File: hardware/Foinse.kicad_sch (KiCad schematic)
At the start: 150 parts, among them J1 Conn_02x03_Odd_Even, J10 Conn_02x03_Odd_Even, J2 2060-1452, J3 ESQ-110-14-G-D, J4 PJ-002AH, J5 2060-1452/998-404, J8 2601-1108, J9 USB_C_Receptacle_USB2.0_16P, Q1 AO3400A, Q10 AO3400A, Q11 AO3400A, Q12 AO3400A, Q13 AO3400A, Q14 AO3400A, Q2 AO3400A, Q3 AO3400A, Q4 AO3400A, Q5 AO3400A, Q6 AO3400A, Q7 AO3400A, Q8 AO3400A, Q9 AO3400A, U1 STM32F072C8Tx, U10 LTV-817, U11 LTV-817, U12 LTV-817, U13 LTV-817, U14 USBLC6-2SC6, U15 INA239AIDGSR, U16 INA239AIDGSR, U17 LTC4412xS6, U18 LTV-817, U19 TPS56A37RPAR, U2 TLV70433DBVT, U3 LTV-817, U4 TJA1051T-3, U5 TPS563203, U7 LTV-817, U8 LTV-817, U9 LTV-817

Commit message: folders are indded cool
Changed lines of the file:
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@@
 		(exclude_from_sim no)
 		(at 476.25 21.59 0)
-		(size -99.06 260.35)
+		(size 99.06 260.35)
 		(margins 0.9525 0.9525 0.9525 0.9525)
 		(stroke

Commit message: minor changes
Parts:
- removed C30, C31, C33: 1 uF, Capacitor_SMD:C_0402_1005Metric, symbol Device:C
- removed D1, D11, D3, D5, D7: RED LED, LED_SMD:LED_0402_1005Metric, symbol Device:LED
- removed D2, D4, D6, D8: GREEN LED, LED_SMD:LED_0402_1005Metric, symbol Device:LED
- removed J1, J10: Conn_02x03_Odd_Even, Connector_PinHeader_1.00mm:PinHeader_2x03_P1.00mm_Vertical, symbol Connector_Generic:Conn_02x03_Odd_Even
- removed J2: 2060-1452, Foinse Footprints:WAG, symbol Wago_2060-1452 998-404:2060-1452_998-404
- removed J3: ESQ-110-14-G-D, Foinse Footprints:SAMTEC_ESQ-110-14-G-D, symbol ESQ-110-X-X-D:ESQ-110-X-X-D
- removed J5: 2060-1452/998-404, Foinse Footprints:WAG, symbol Wago_2060-1452 998-404:2060-1452_998-404
- removed J8: 2601-1108, Foinse Footprints:CONN8_2601-1108_WAG, symbol Wago_2601-1104:2601-1108
- removed J9: USB_C_Receptacle_USB2.0_16P, Connector_USB:USB_C_Receptacle_G-Switch_GT-USB-7010ASV, symbol Connector:USB_C_Receptacle_USB2.0_16P
- removed Q1, Q10, Q11, Q12, Q13, Q14, Q2, Q3, Q4, Q5, Q6, Q7, Q8, Q9: AO3400A, Package_TO_SOT_SMD:SOT-23, symbol Transistor_FET:AO3400A
- removed R10, R30, R39: 2 kΩ, Resistor_SMD:R_0402_1005Metric, symbol Device:R
- removed R11, R40: 4.7 kΩ, Resistor_SMD:R_0402_1005Metric, symbol Device:R
- removed R12, R14, R16, R23, R25, R32, R34, R48, R6: 10k Ω, Resistor_SMD:R_0402_1005Metric, symbol Device:R
- removed R13, R19, R28, R37: 1k Ω, Resistor_SMD:R_0402_1005Metric, symbol Device:R
- removed R15, R24, R33, R47: 220 Ω, Resistor_SMD:R_0402_1005Metric, symbol Device:R
- removed R18, R22, R27, R31, R36, R49, R8: 4.7k Ω, Resistor_SMD:R_0402_1005Metric, symbol Device:R
- removed R20: 6k Ω, Resistor_SMD:R_0402_1005Metric, symbol Device:R
- removed R21: 2k Ω, Resistor_SMD:R_0402_1005Metric, symbol Device:R
- removed R29, R38, R9: 6 kΩ, Resistor_SMD:R_0402_1005Metric, symbol Device:R
- removed R41, R42: 5.1K, Resistor_SMD:R_0402_1005Metric, symbol Device:R
- removed R43, R44: 10K, Resistor_SMD:R_0402_1005Metric, symbol Device:R
- removed U10, U11, U12, U13, U18, U3, U7, U8, U9: LTV-817, Foinse Footprints:SO4_TOS, symbol Isolator:LTV-817
- removed U14: USBLC6-2SC6, Package_TO_SOT_SMD:SOT-23-6, symbol Power_Protection:USBLC6-2SC6
- added J1: ESQ-110-X-X-D, SAMTEC_ESQ-110-14-G-D, symbol ESQ-110-X-X-D:ESQ-110-X-X-D
- added J2: XT30PW-M, footprints:AMASS_XT30PW-M, symbol XT30PW-M:XT30PW-M
- added J6: JTAG-10 PIN, Connector_IDC:IDC-Header_2x05_P2.54mm_Vertical, symbol Connector_Generic_MountingPin:Conn_01x10_MountingPin
- C32: value 1 uF -> 100nF
- R5: value 220 Ω -> 10kΩ
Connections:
- net Aux1 neg is gone; now on net GND: C32.2
- net VBAT_AUX1 is gone; now on net NRST: C32.1
- net 3.3V: now also J6.7 (Pin_7), J6.8 (Pin_8)
- net GND: now also R5.2, J1.03, J1.04, J1.07, J1.08, J1.14, J1.19, J1.20, J2.N, J6.5 (Pin_5), J6.6 (Pin_6)
- net NRST: now also J1.17, J6.1 (Pin_1)
- net SWDIO: now also J1.15, J6.4 (Pin_4)
- net at MOSFET1.2 (D), U17.1 (VIN): now also J2.P
- net at U1.44 (BOOT0): now also R5.1
- net AUX1_FIRE: no longer names the net of U1.41 (PB5)
- net AUX1_SEAT: no longer names the net of U1.25 (PB12)
- net AUX2_FIRE: no longer names the net of U1.42 (PB6)
- net AUX2_SEAT: no longer names the net of U1.26 (PB13)
- net DROGUE_FIRE: no longer names the net of U1.39 (PB3)
- net DROGUE_FIRE: no longer R5.1
- net DROGUE_SEAT: no longer names the net of U1.21 (PB10)
- net MAIN_FIRE: no longer names the net of U1.40 (PB4)
- net MAIN_SEAT: no longer names the net of U1.22 (PB11)
- net Mode_sel: no longer names the net of U1.45 (PB8)
- net PYRO_ON: no longer names the net of U1.43 (PB7)
- net SWCLK renamed SWCLK3
- net SWCLK3: now also J1.11, J6.2 (Pin_2)
- new net 5V_LOGIC: J1.05, J1.06
- new net 5v_SERVO: J1.01, J1.02
- new net CAN_o+: J1.16
- new net CAN_o-: J1.18
- no-connect marks 6 -> 12
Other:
- note added: "Connector_IDC:IDC-Header_2x05_P2.54mm_Vertical"
- note added: "what is the current and voltage rating for this?"
- note removed: "E-Match Trigger Circuit"
- note removed: "Pyro Connectors"
- note removed: "USB-C"
- note removed: "USB-C & mode select"
- moved on the sheet: C1, C10, C11, C12, C13, C14, C15, C16, C17, C18, C19, C2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

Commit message: minor changes
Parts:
- added R4: 10kΩ, Resistor_SMD:R_0402_1005Metric, symbol Device:R
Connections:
- net 3.3V: now also R4.2
- net NRST: now also R4.1
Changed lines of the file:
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@@
 	)
 	(junction
+		(at 152.4 121.92)
+		(diameter 0)
+		(color 0 0 0 0)
+	)
+	(junction
 		(at 133.1412 302.1058)
 		(diameter 0)
@@
 	(wire
 		(pts
+			(xy 152.4 132.08) (xy 152.4 130.81)
+		)
+		(stroke
+			(width 0)
+			(type default)
+		)
+	)
+	(wire
+		(pts
 			(xy 414.383 197.3473) (xy 408.033 197.3473)
 		)
@@
 	(wire
 		(pts
+			(xy 152.4 123.19) (xy 152.4 121.92)
+		)
+		(stroke
+			(width 0)
+			(type default)
+		)
+	)
+	(wire
+		(pts
 			(xy 179.07 102.87) (xy 179.07 104.14)
 		)
@@
 	(wire
 		(pts
-			(xy 157.48 121.92) (xy 161.29 121.92)
+			(xy 148.59 121.92) (xy 152.4 121.92)
 		)
 		(stroke
@@
 	(wire
 		(pts
+			(xy 152.4 121.92) (xy 161.29 121.92)
+		)
+		(stroke
+			(width 0)
+			(type default)
+		)
+	)
+	(wire
+		(pts
 			(xy 380.093 184.6473) (xy 381.363 184.6473)
 		)
@@
 	(global_label "NRST"
 		(shape input)
-		(at 157.48 121.92 180)
+		(at 148.59 121.92 180)
 		(fields_autoplaced yes)
 		(effects
@@
 		)
 		(property "Intersheetrefs" "${INTERSHEET_REFS}"
-			(at 149.7172 121.92 0)
+			(at 140.8272 121.92 0)
 			(effects
 				(font
@@
 		)
 	)
+	(global_label "3.3V"
+		(shape input)
+		(at 152.4 132.08 180)
+		(fields_autoplaced yes)
+		(effects
+			(font
+				(size 1.27 1.27)
+			)
+			(justify right)
+		)
+		(property "Intersheetrefs" "${INTERSHEET_REFS}"
+			(at 145.3024 132.08 0)
+			(effects
+				(font
+					(size 1.27 1.27)
+				)
+				(justify right)
+				(hide yes)
+			)
+		)
+	)
 	(global_label "VBAT_BS"
 		(shape input)
@@
 					(unit 1)
 				)
+			)
+		)
+	)
+	(symbol
+		(lib_id "Device:R")
+		(at 152.4 127 0)
+		(unit 1)
+		(exclude_from_sim no)
+		(in_bom yes)
+		(on_board yes)
+		(dnp no)
+		(property "Reference" "R4"
+			(at 150.114 127 90)
+			(effects
+				(font
+					(size 1.27 1.27)
+				)
+			)
+		)
+		(property "Value" "10kΩ"
+			(at 154.94 127 90)
+			(effects
+				(font
+					(size 1.27 1.27)
+				)
+			)
+		)
+		(property "Footprint" "Resistor_SMD:R_0402_1005Metric"
+			(at 150.622 127 90)
+			(effects
+				(font
+					(size 1.27 1.27)
+				)
+				(hide yes)
+			)
+		)
+		(property "Datasheet" "~"
+			(at 152.4 127 0)
+			(effects
+				(font
+					(size 1.27 1.27)
+				)
+				(hide yes)
+			)
+		)
+		(property "Description" "Resistor"
+			(at 152.4 127 0)
+			(effects
+				(font
+					(size 1.27 1.27)
+				)
+				(hide yes)
+			)
+		)
+		(pin "2"
+		)
+		(pin "1"
+		)
+		(instances
+			(project "Foinse"
+				(path "/e25e400c-9bc4-4e0b-8f6d-7db79788ea60"
+					(reference "R4")
+					(unit 1)
+				)

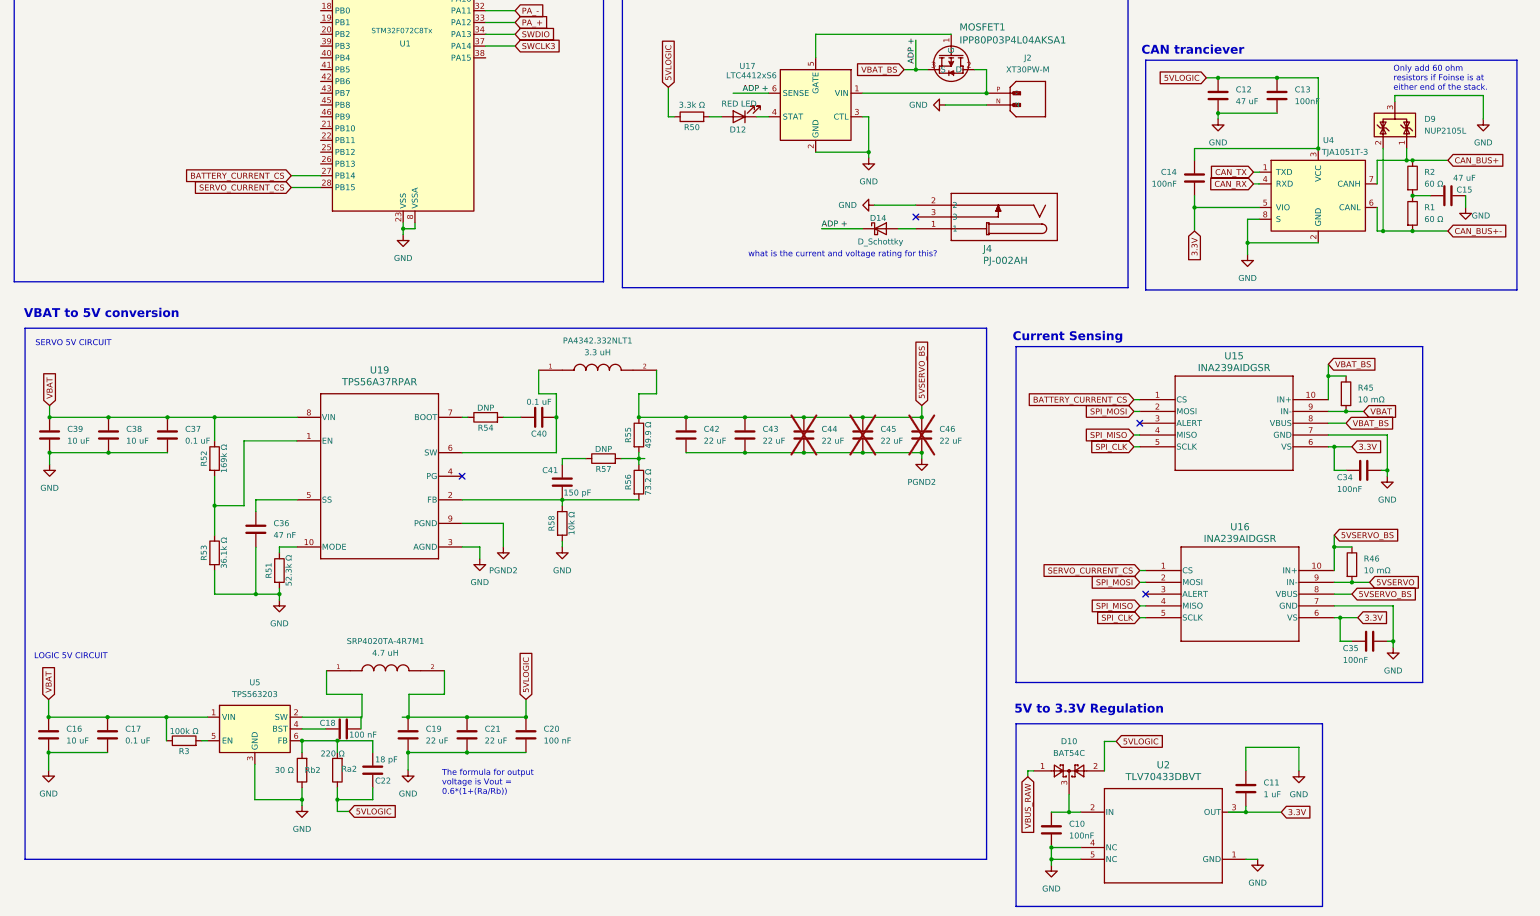
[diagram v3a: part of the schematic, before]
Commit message: 5v logic routed
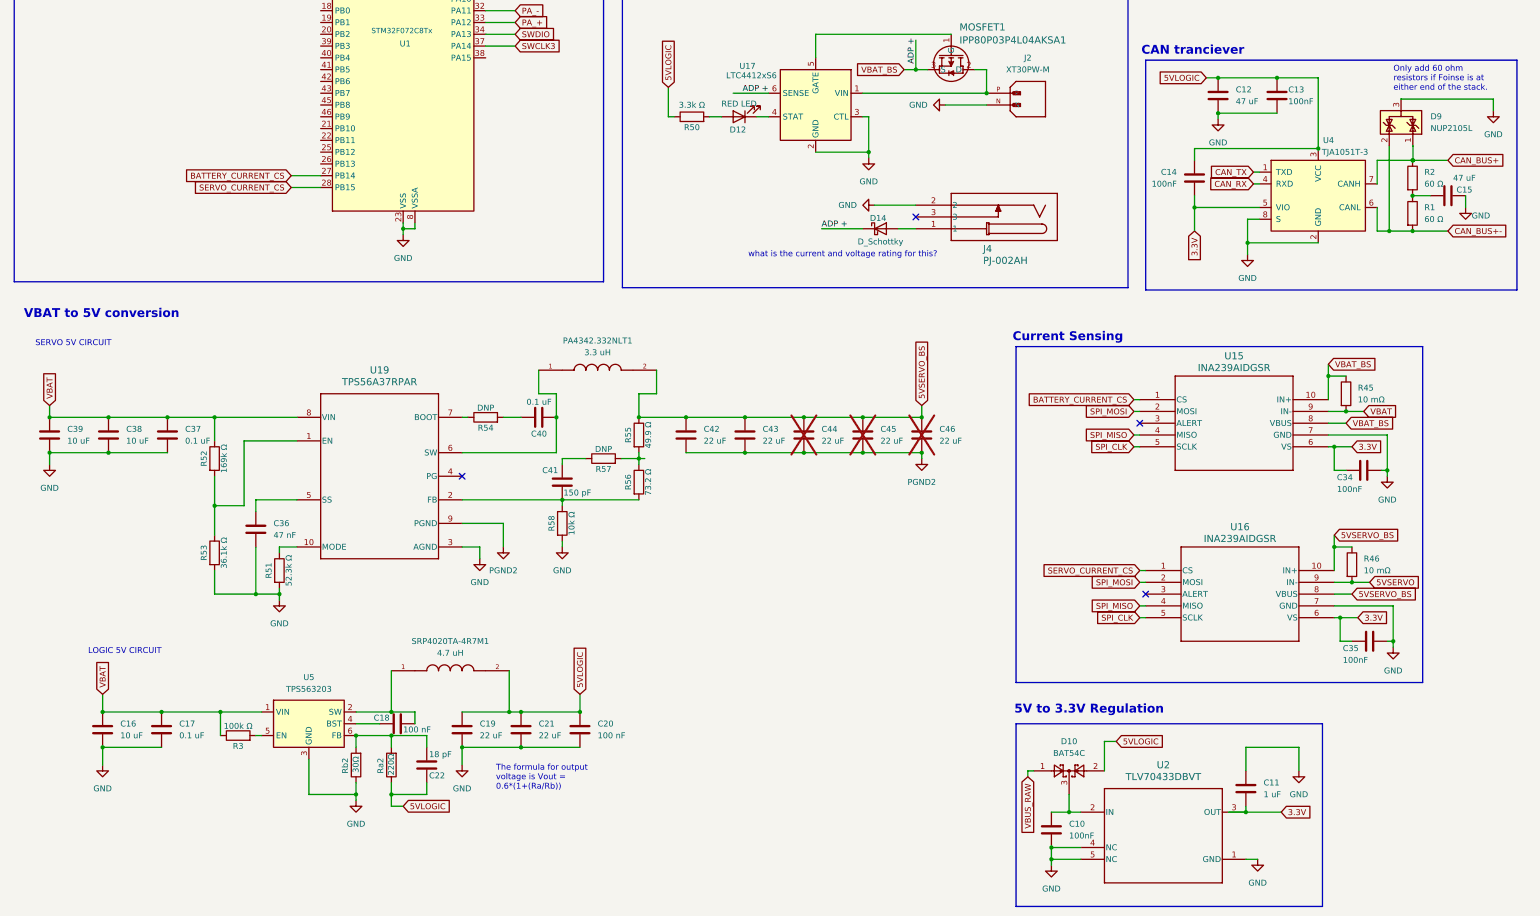
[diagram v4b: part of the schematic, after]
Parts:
- J1: footprint SAMTEC_ESQ-110-14-G-D -> footprints:SAMTEC_ESQ-110-14-G-D
- Ra2: value 220 Ω -> 220Ω
- Rb2: value 30 Ω -> 30Ω
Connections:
- net 5VLOGIC: now also SRP4020TA-4R7M1.2
- net at SRP4020TA-4R7M1.1: now also C18.1, U5.2 (SW)
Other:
- moved on the sheet: C16, C17, C18, C19, C20, C21, C22, D9, R3, Ra2, Rb2, SRP4020TA-4R7M1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

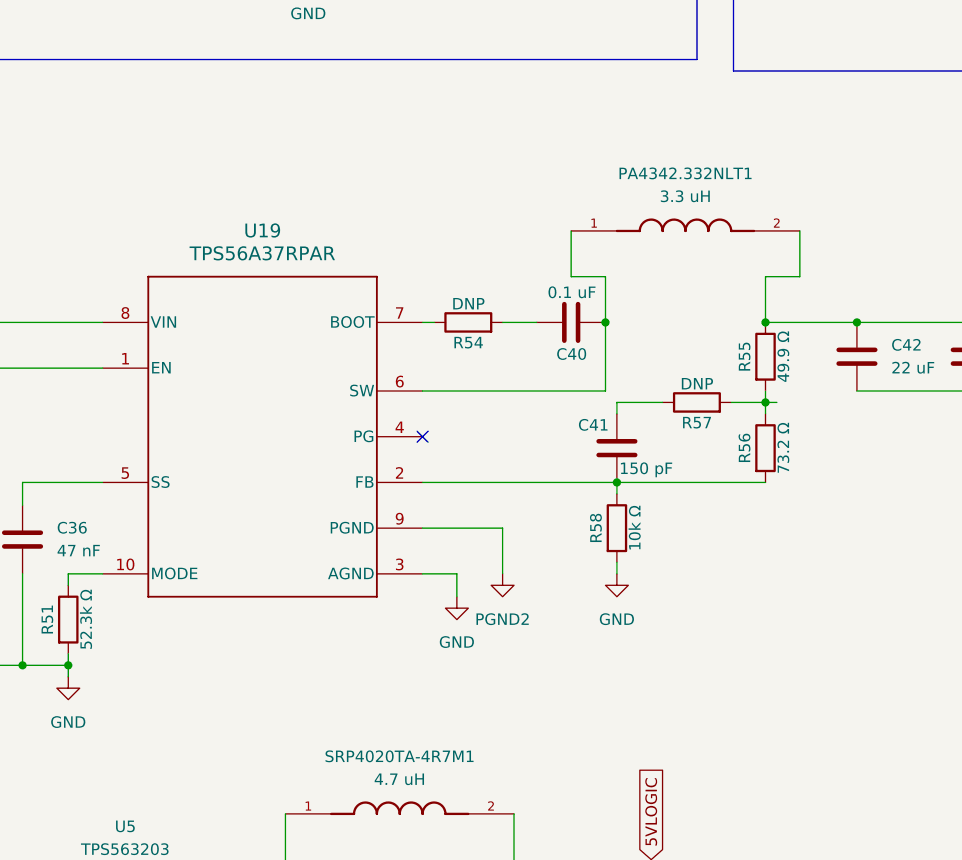
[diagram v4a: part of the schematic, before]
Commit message: new inductor
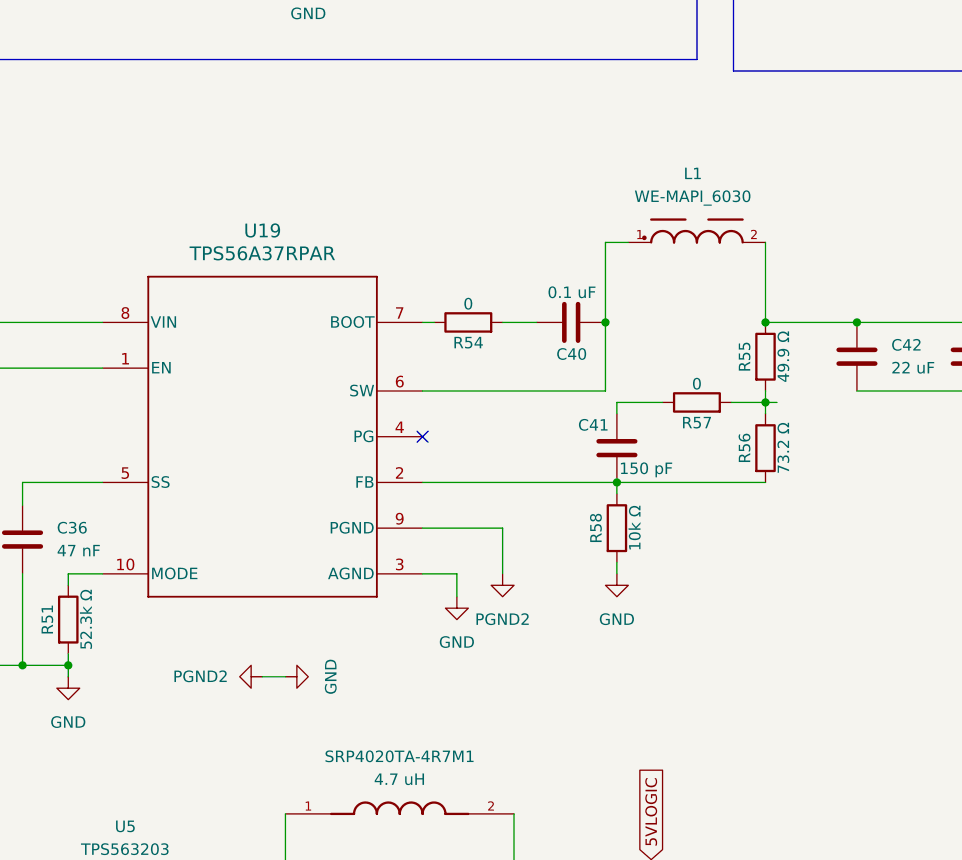
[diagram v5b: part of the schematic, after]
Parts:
- removed PA4342.332NLT1: 3.3 uH, Foinse Footprints:IND_PA4342.332NLT, symbol PA4342.332NLT:PA4342.332NLT
- added L1: WE-MAPI_6030, footprints:WE-MAPI_6030, symbol WE-MAPI_6030:WE-MAPI_6030
- R54, R57: value DNP -> 0
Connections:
- net PGND2 is gone; now on net GND: C42.2, C43.2, C44.2, C45.2, C46.2, U19.9 (PGND)
- net 5VSERVO_BS: now also L1.2
- net at C40.2, U19.6 (SW): now also L1.1
